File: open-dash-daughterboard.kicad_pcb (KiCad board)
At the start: 2 copper layers, 165.5 x 107.3 mm, 161 parts, among them J4 Conn_02x06_Odd_Even, P1 CONN_01X04, P2 CONN_01X02, P4 CONN_01X04, Q1 Q_NPN_BEC, Q2 Q_NJFET_DGS, Q3 Q_NJFET_DGS, Q4 Q_NPN_BCE, Q5 Q_PNP_BCE, U1 LM2576-ADJ, U10 Power-Monitor-INA219, U11 TDA7297, U12 Si4740, U13 A2235-H, U14 molex-2x4-5.7mm, U15 radio-housing-mounts, U16 molex-2x4-5.7mm, U17 USB_IC-CP2104, U18 74LVC1G17SE-7, U19 OPA1662, U2 LM2576-ADJ, U3 LM2576-ADJ, U4 LM2576-ADJ, U5 REG-3.3v, U6 ESP-WROOM-32, U7 molex-2x4-5.7mm, U8 MCP2551-I_SN, U9 SI7020-A20

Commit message: update
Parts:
- moved U14 5.23 mm to (141.9, 121.5)
- moved R5 1.00 mm to (107.9, 53.0)
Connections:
- U11 pad 14: /FL_AUDIO_OUT- -> /FR_AUDIO_OUT-
- U14 pad 2: /FL_AUDIO_OUT+ -> /FR_AUDIO_OUT+
- U14 pad 3: /FR_AUDIO_OUT+ -> /FL_AUDIO_OUT+
- U14 pad 5: /FL_AUDIO_OUT- -> /FR_AUDIO_OUT-
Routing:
- net /5V: track 54.0 -> 221.7 mm
- net /SOFT_POWER: track 14.4 -> 181.8 mm, vias 0 -> 5
- net /3v3: track 146.9 -> 310.0 mm, vias 0 -> 7
- net /SDA: track 16.9 -> 159.1 mm, vias 2 -> 14
- net /SCL: track 10.7 -> 127.6 mm, vias 0 -> 8
- net /PROG: track 6.29 -> 99.8 mm, vias 0 -> 3
- net /EN_AUDIO: track 0.00 -> 79.9 mm, vias 0 -> 2
- net /FACTORY: track 4.10 -> 63.1 mm, vias 0 -> 2
- net /AUDIO_POWER: track 52.4 -> 109.0 mm, vias 0 -> 1
- net /EN_MAIN: track 13.1 -> 68.2 mm, vias 0 -> 2
- net /CAN_RX: track 0.00 -> 52.5 mm, vias 0 -> 2
- net /FM Radio/am_passive_ant_en: track 4.00 -> 49.4 mm, vias 0 -> 2
- net /RXD: track 0.00 -> 43.9 mm, vias 0 -> 2
- net /STBY_AUDIO: track 0.00 -> 43.1 mm, vias 0 -> 2
- net /BATTERY: track 151.6 -> 193.9 mm, vias 0 -> 2
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
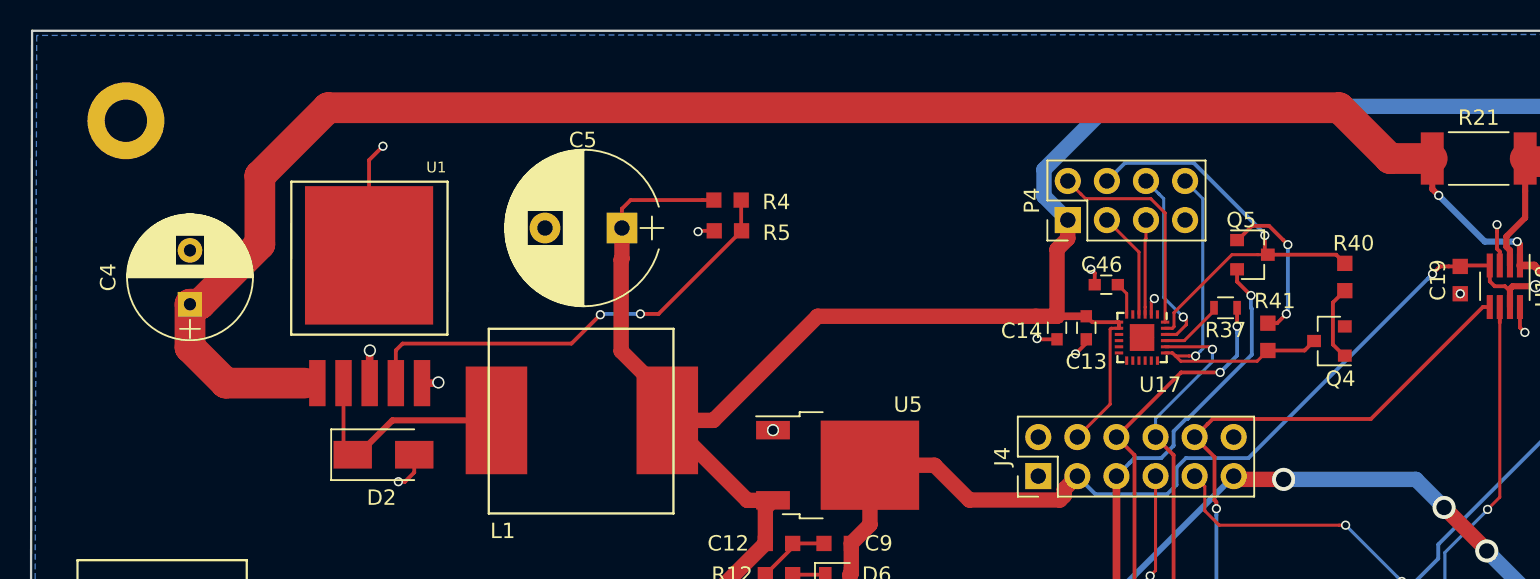
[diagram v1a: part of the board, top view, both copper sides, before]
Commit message: rearranged traces
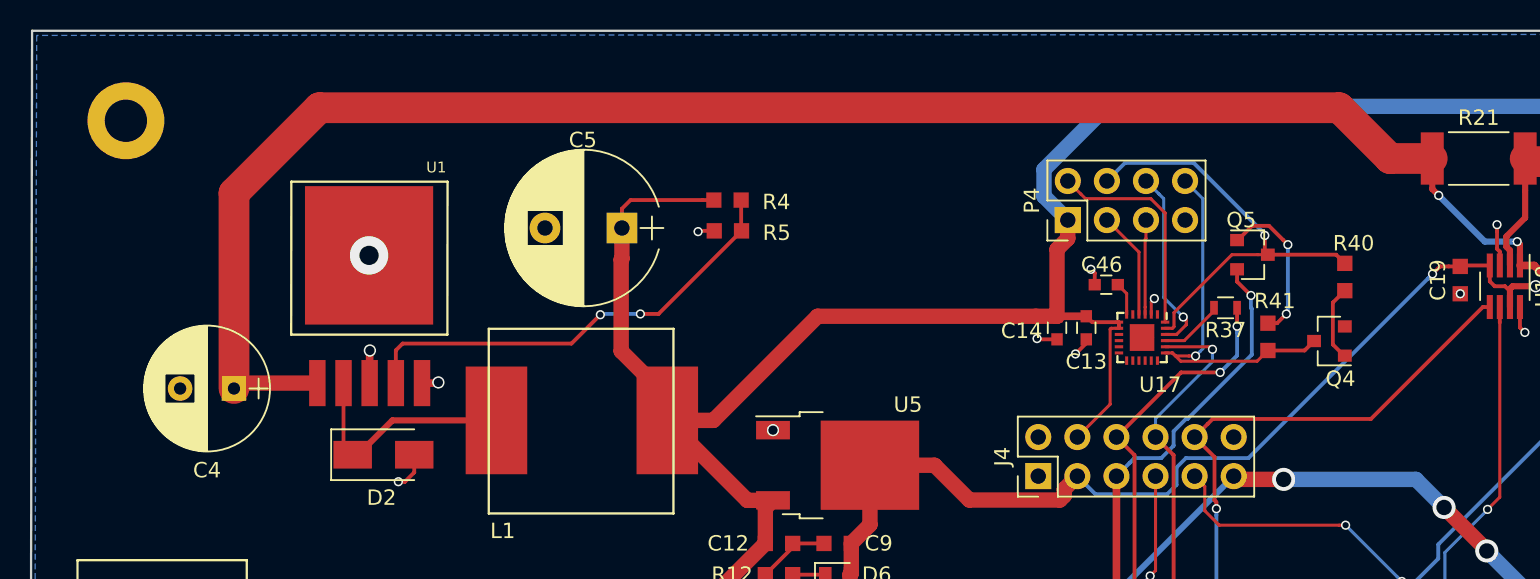
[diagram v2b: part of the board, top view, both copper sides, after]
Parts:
- moved C4 6.18 mm to (75.8, 63.2), turned to 180 degrees
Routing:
- net AGND: track 155.5 -> 148.0 mm
- net /BATTERY: track 193.9 -> 192.5 mm

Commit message: update
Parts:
- moved R13 2.42 mm to (151.0, 94.9), turned to 0 degrees
- moved L5 1.33 mm to (213.9, 123.9)
- moved R14 1.21 mm to (151.0, 92.4), turned to 0 degrees
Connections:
- AMF_Antenna1 pad 2: GNDA -> AGND
- C22 pad 1: /AUDIO_POWER -> AGND
- C22 pad 2: AGND -> /AUDIO_POWER
- GPS_ANT1 pad 2: GNDA -> AGND
- U14 pad 5: /FR_AUDIO_OUT- -> /FL_AUDIO_OUT-
- U14 pad 8: /FL_AUDIO_OUT- -> /FR_AUDIO_OUT-
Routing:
- net /3v3: track 310.0 -> 400.2 mm, vias 7 -> 11
- net /EN_DISPLAY: track 13.2 -> 62.5 mm, vias 2 -> 6
- net /CAN_TX: track 0.00 -> 49.2 mm, vias 0 -> 4
- net /EN_ESP: track 16.5 -> 57.6 mm, vias 2 -> 6
- net /BATTERY: track 192.5 -> 233.5 mm
- net /FR_AUDIO_OUT-: track 0.00 -> 39.8 mm
- net /FL_AUDIO_OUT+: track 0.46 -> 38.2 mm
- net /FR_AUDIO_OUT+: track 0.00 -> 31.8 mm
- net /FL_AUDIO_OUT-: track 0.00 -> 31.5 mm
- net /SDA: track 159.1 -> 129.8 mm, vias 14 -> 9
- net /STBY_AUDIO: track 43.1 -> 60.3 mm, vias 2 -> 8
- net /EN_AUDIO: track 79.9 -> 89.6 mm
- net /CAN_RX: track 52.5 -> 61.8 mm, vias 2 -> 6
- net Net-(D2-Pad1): track 15.2 -> 21.0 mm
- net /V_MAIN: track 36.3 -> 31.0 mm
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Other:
- board text added: "3v3"
- board text added: "5V"
- board text added: "BATT"
- board text added: "CAM +"
- board text added: "CAM --"
- board text added: "CAM_S"
- board text added: "CAN +"
- board text added: "CAN -"
- board text added: "DCD"
- board text added: "DSR"
- board text added: "DTR"
- board text added: "D_N"
- board text added: "D_P"
- board text added: "FACT"
- board text added: "FL OUT +"
- board text added: "FL OUT -"
- board text added: "FR OUT +"
- board text added: "FR OUT -"
- board text added: "GND"
- board text added: "IN2"
- board text added: "L MAIN"
- board text added: "NC"
- board text added: "OUT2+"
- board text added: "OUT2-"
- board text added: "PROG"
- board text added: "R MAIN"
- board text added: "RTS"
- board text added: "RXD"
- board text added: "SCL"
- board text added: "SDA"
- board text added: "SOFT P"
- board text added: "SOFT_P"
- board text added: "TXD"
- board text added: "VCC"

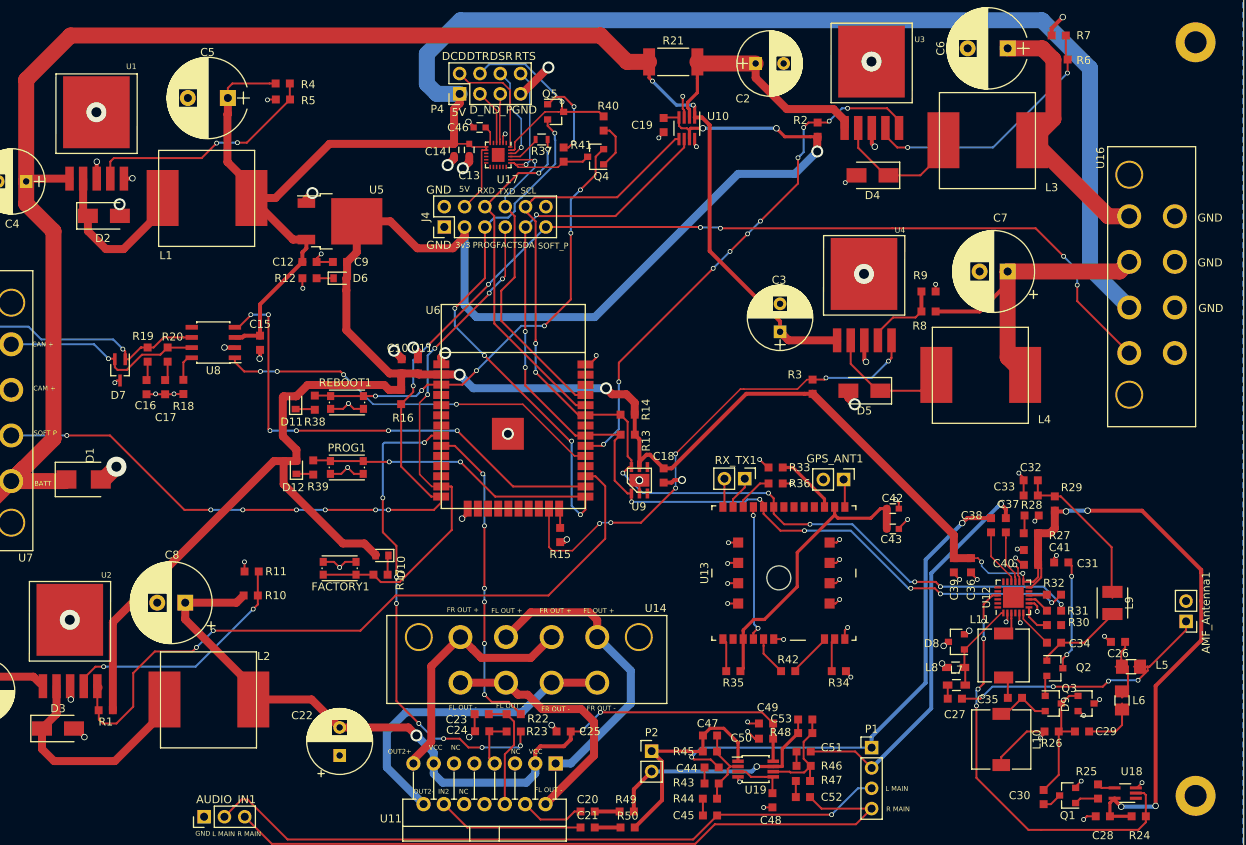
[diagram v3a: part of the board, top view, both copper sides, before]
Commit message: final update silk screen
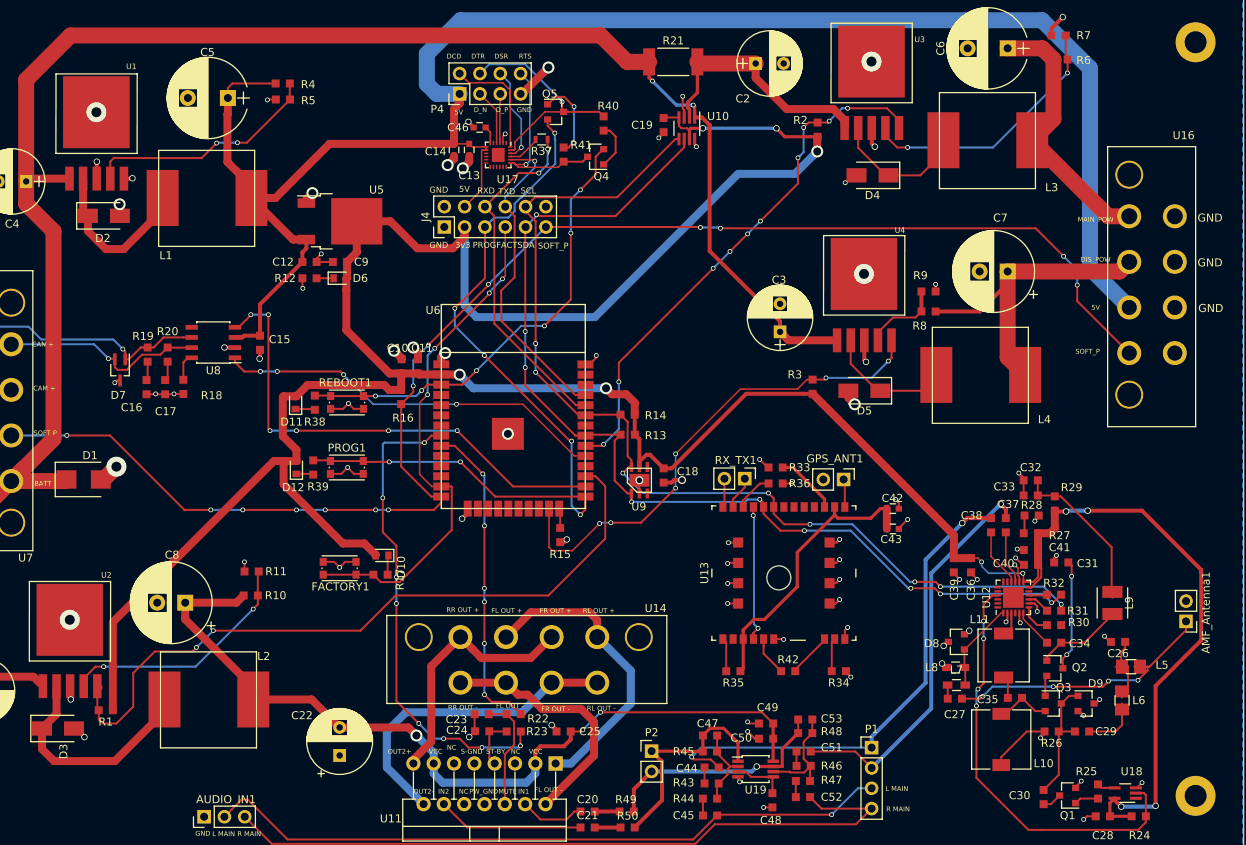
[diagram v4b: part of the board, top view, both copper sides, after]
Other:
- board text added: "DIS_POW"
- board text added: "IN1"
- board text added: "MAIN_POW"
- board text added: "MUTE"
- board text added: "PW_GND"
- board text added: "RL OUT +"
- board text added: "RL OUT -"
- board text added: "RR OUT +"
- board text added: "RR OUT -"
- board text added: "S-GND"
- board text added: "ST-BY"
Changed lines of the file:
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@@
   (general
     (thickness 1.6)
-    (drawings 56)
+    (drawings 65)
     (tracks 1520)
     (zones 0)
@@
     (tags "resistor handsolder")
     (attr smd)
-    (fp_text reference R48 (at 3.1 0.1 180) (layer F.SilkS)
+    (fp_text reference R48 (at -3.3 0.2 180) (layer F.SilkS)
       (effects (font (size 1 1) (thickness 0.15)))
     )
@@
     (tags "Diode SMB (DO-214AA)")
     (attr smd)
-    (fp_text reference D1 (at 0.8 -3 -90) (layer F.SilkS)
+    (fp_text reference D1 (at 0.8 -3 180) (layer F.SilkS)
       (effects (font (size 1 1) (thickness 0.15)))
     )
@@
     (tags "capacitor handsolder")
     (attr smd)
-    (fp_text reference C15 (at -2.33 0) (layer F.SilkS)
+    (fp_text reference C15 (at -0.41 -2.45) (layer F.SilkS)
       (effects (font (size 1 1) (thickness 0.15)))
     )
@@
     (tags "capacitor handsolder")
     (attr smd)
-    (fp_text reference C16 (at 2.29 0.13) (layer F.SilkS)
+    (fp_text reference C16 (at 2.54 1.86) (layer F.SilkS)
       (effects (font (size 1 1) (thickness 0.15)))
     )
@@
     (tags "capacitor handsolder")
     (attr smd)
-    (fp_text reference C17 (at 3.78 -0.07) (layer F.SilkS)
+    (fp_text reference C17 (at 3.04 -0.07) (layer F.SilkS)
       (effects (font (size 1 1) (thickness 0.15)))
     )
@@
     (tags "capacitor handsolder")
     (attr smd)
-    (fp_text reference C18 (at -2.4 0) (layer F.SilkS)
+    (fp_text reference C18 (at -0.5 -3) (layer F.SilkS)
       (effects (font (size 1 1) (thickness 0.15)))
     )
@@
     (tags "resistor handsolder")
     (attr smd)
-    (fp_text reference R13 (at 2.2875 0.762 90) (layer F.SilkS)
+    (fp_text reference R13 (at 3.4875 0.1 180) (layer F.SilkS)
       (effects (font (size 1 1) (thickness 0.15)))
     )
@@
     (tags "resistor handsolder")
     (attr smd)
-    (fp_text reference R14 (at 2.2875 -0.635 90) (layer F.SilkS)
+    (fp_text reference R14 (at 3.5 0.1 180) (layer F.SilkS)
       (effects (font (size 1 1) (thickness 0.15)))
     )
@@
     (tags "resistor handsolder")
     (attr smd)
-    (fp_text reference R18 (at 2.41 -0.01) (layer F.SilkS)
+    (fp_text reference R18 (at 1.07 -3.53) (layer F.SilkS)
       (effects (font (size 1 1) (thickness 0.15)))
     )
@@
     (tags "resistor handsolder")
     (attr smd)
-    (fp_text reference R20 (at -2.22 -0.6) (layer F.SilkS)
+    (fp_text reference R20 (at -2.8875 0) (layer F.SilkS)
       (effects (font (size 1 1) (thickness 0.15)))
     )
@@
     (tags "Diode SMA (DO-214AC)")
     (attr smd)
-    (fp_text reference D3 (at 0 -2.5) (layer F.SilkS)
+    (fp_text reference D3 (at 0.704 2.871 90) (layer F.SilkS)
       (effects (font (size 1 1) (thickness 0.15)))
     )
@@
   (module open-automation:molex-2x4-5.7mm (layer F.Cu)
     (at 215 72.9 90)
-    (fp_text reference U16 (at 12.6 -4.9 90) (layer F.SilkS)
+    (fp_text reference U16 (at 15.4 5.5 180) (layer F.SilkS)
       (effects (font (size 1 1) (thickness 0.15)))
     )
@@
     (tags "Choke SMD")
     (attr smd)
-    (fp_text reference L10 (at 0 -4.45 270) (layer F.SilkS)
+    (fp_text reference L10 (at 3 -5.3) (layer F.SilkS)
       (effects (font (size 1 1) (thickness 0.15)))
     )
@@
     (tags SOT-23)
     (attr smd)
-    (fp_text reference Q2 (at 3.6 -0.1) (layer F.SilkS)
+    (fp_text reference Q2 (at 3.1 -0.1) (layer F.SilkS)
       (effects (font (size 1 1) (thickness 0.15)))
     )
@@
     (tags SOT-23)
     (attr smd)
-    (fp_text reference Q3 (at 2 -1.9) (layer F.SilkS)
+    (fp_text reference Q3 (at 1.3 -2) (layer F.SilkS)
       (effects (font (size 1 1) (thickness 0.15)))
     )
@@
     (tags SOT-23)
     (attr smd)
-    (fp_text reference D9 (at -2.6 0.1 -270) (layer F.SilkS)
+    (fp_text reference D9 (at 1.2 -2.5 -180) (layer F.SilkS)
       (effects (font (size 1 1) (thickness 0.15)))
     )
@@
     (tags "capacitor handsolder")
     (attr smd)
-    (fp_text reference C53 (at -3 -0.1) (layer F.SilkS)
+    (fp_text reference C53 (at 3.3 -0.1) (layer F.SilkS)
       (effects (font (size 1 1) (thickness 0.15)))
     )
@@
     (pad M thru_hole circle (at 10.5 -1.3) (size 3.5 3.5) (drill 3) (layers *.Cu *.Mask))
   )
+  (gr_text MAIN_POW (at 209.5 68) (layer F.SilkS)
+    (effects (font (size 0.6 0.6) (thickness 0.15)))
+  )
+  (gr_text DIS_POW (at 209.5 73) (layer F.SilkS)
+    (effects (font (size 0.6 0.6) (thickness 0.15)))
+  )
+  (gr_text 5V (at 209.5 79) (layer F.SilkS)
+    (effects (font (size 0.6 0.6) (thickness 0.15)))
+  )
+  (gr_text SOFT_P (at 208.5 84.5) (layer F.SilkS)
+    (effects (font (size 0.6 0.6) (thickness 0.15)))
+  )
+  (gr_text S-GND (at 131.5 134.5) (layer F.SilkS)
+    (effects (font (size 0.6 0.6) (thickness 0.15)))
+  )
+  (gr_text ST-BY (at 134.5 134.5) (layer F.SilkS)
+    (effects (font (size 0.6 0.6) (thickness 0.15)))
+  )
+  (gr_text IN1 (at 138 139.5) (layer F.SilkS)
+    (effects (font (size 0.6 0.6) (thickness 0.15)))
+  )
+  (gr_text MUTE (at 136 139.5) (layer F.SilkS)
+    (effects (font (size 0.6 0.6) (thickness 0.15)))
+  )
+  (gr_text PW_GND (at 133 139.5) (layer F.SilkS)
+    (effects (font (size 0.6 0.6) (thickness 0.15)))
+  )
   (gr_text OUT2+ (at 122.5 134.5) (layer F.SilkS)
     (effects (font (size 0.6 0.6) (thickness 0.15)))
@@
     (effects (font (size 0.6 0.6) (thickness 0.15)))
   )
-  (gr_text VCC (at 127 134) (layer F.SilkS)
+  (gr_text VCC (at 127 134.5) (layer F.SilkS)
     (effects (font (size 0.6 0.6) (thickness 0.15)))
   )
-  (gr_text NC (at 129.5 134) (layer F.SilkS)
+  (gr_text NC (at 129 134) (layer F.SilkS)
     (effects (font (size 0.6 0.6) (thickness 0.15)))
   )
@@
     (effects (font (size 0.6 0.6) (thickness 0.15)))
   )
-  (gr_text "FL OUT -" (at 130.4 129) (layer F.SilkS)
+  (gr_text "RR OUT -" (at 130.4 129) (layer F.SilkS)
     (effects (font (size 0.6 0.6) (thickness 0.15)))
   )
@@
     (effects (font (size 0.6 0.6) (thickness 0.15)))
   )
-  (gr_text "FR OUT -" (at 147.7 129.1) (layer F.SilkS)
+  (gr_text "RL OUT -" (at 147.7 129.1) (layer F.SilkS)
     (effects (font (size 0.6 0.6) (thickness 0.15)))
   )
-  (gr_text "FL OUT +" (at 147.4 116.9) (layer F.SilkS)
+  (gr_text "RL OUT +" (at 147.4 116.9) (layer F.SilkS)
     (effects (font (size 0.6 0.6) (thickness 0.15)))
   )
@@
     (effects (font (size 0.6 0.6) (thickness 0.15)))
   )
-  (gr_text "FR OUT +" (at 130.4 116.8) (layer F.SilkS)
+  (gr_text "RR OUT +" (at 130.4 116.8) (layer F.SilkS)
     (effects (font (size 0.6 0.6) (thickness 0.15)))
   )
@@
   )
   (gr_text GND (at 127.4 71.2) (layer F.SilkS)
-    (effects (font (size 1 1) (thickness 0.25)))
+    (effects (font (size 0.75 0.75) (thickness 0.1875)))
   )
   (gr_text GND (at 127.4 64.3) (layer F.SilkS)
-    (effects (font (size 1 1) (thickness 0.25)))
+    (effects (font (size 0.75 0.75) (thickness 0.1875)))
   )
   (gr_text GND (at 64.1 100.8) (layer F.SilkS)
@@
   )
   (gr_text GND (at 138.1 54.3) (layer F.SilkS)
-    (effects (font (size 1 1) (thickness 0.25)))
+    (effects (font (size 0.6 0.6) (thickness 0.15)))
   )
   (gr_text D_P (at 135.3 54.3) (layer F.SilkS)
-    (effects (font (size 1 1) (thickness 0.25)))
+    (effects (font (size 0.6 0.6) (thickness 0.15)))
   )
   (gr_text D_N (at 132.6 54.3) (layer F.SilkS)
-    (effects (font (size 1 1) (thickness 0.25)))
+    (effects (font (size 0.6 0.6) (thickness 0.15)))
   )
   (gr_text 5V (at 129.9 54.6) (layer F.SilkS)
-    (effects (font (size 1 1) (thickness 0.25)))
+    (effects (font (size 0.6 0.6) (thickness 0.15)))
   )
   (gr_text DSR (at 135.2 47.6) (layer F.SilkS)
-    (effects (font (size 1 1) (thickness 0.25)))
+    (effects (font (size 0.6 0.6) (thickness 0.15)))
   )
   (gr_text DTR (at 132.3 47.6) (layer F.SilkS)
-    (effects (font (size 1 1) (thickness 0.25)))
+    (effects (font (size 0.6 0.6) (thickness 0.15)))
   )
   (gr_text DCD (at 129.3 47.6) (layer F.SilkS)
-    (effects (font (size 1 1) (thickness 0.25)))
+    (effects (font (size 0.6 0.6) (thickness 0.15)))
   )
   (gr_text "RTS\n" (at 138.2 47.6) (layer F.SilkS)
-    (effects (font (size 1 1) (thickness 0.25)))
+    (effects (font (size 0.6 0.6) (thickness 0.15)))
   )
   (gr_line (start 62.7 40) (end 62.5 147.3) (layer Edge.Cuts) (width 0.15))

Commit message: finalizing board
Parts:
- moved C25 22.1 mm to (120.9, 132.6), turned to 270 degrees
- moved C23 0.90 mm to (132.6, 130.7)
- moved R22 0.90 mm to (136.6, 130.7)
- moved R23 0.90 mm to (136.6, 132.9)
- moved C24 0.90 mm to (132.7, 132.9)
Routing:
- net AGND: track 147.5 -> 152.7 mm, vias 88 -> 87
- net /AUDIO_POWER: track 105.0 -> 108.9 mm, vias 3 -> 2
- net Net-(C26-Pad1): track 11.6 -> 10.1 mm
- net Net-(C23-Pad1): track 14.3 -> 13.4 mm
- net /STBY_AUDIO: track 60.3 -> 59.5 mm
- net /MUTE_AUDIO: track 39.9 -> 40.7 mm
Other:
- board text added: "BATTERY"
- board text added: "CAM-"
- board text added: "CAMERA+"
- board text added: "CAN+"
- board text added: "CAN-"
- board text added: "DISPLAY+"
- board text added: "FL+"
- board text added: "FL-"
- board text added: "FR+"
- board text added: "FR-"
- board text added: "L"
- board text added: "L_FM"
- board text added: "L_MAIN"
- board text added: "MAIN+"
- board text added: "OUT1+"
- board text added: "OUT1-"
- board text added: "PWR"
- board text added: "R"
- board text added: "RL+"
- board text added: "RL-"
- board text added: "RR+"
- board text added: "RR-"
- board text added: "R_FM"
- board text added: "R_MAIN"
- board text added: "SOFT_PWR"
- board text added: "STBY"
- board text removed: "BATT"
- board text removed: "CAM +"
- board text removed: "CAM --"
- board text removed: "CAN +"
- board text removed: "CAN -"
- board text removed: "DIS_POW"
- board text removed: "FL OUT +"
- board text removed: "FL OUT -"
- board text removed: "FR OUT +"
- board text removed: "FR OUT -"
- board text removed: "L MAIN"
- board text removed: "MAIN_POW"
- board text removed: "NC"
- board text removed: "PW_GND"
- board text removed: "R MAIN"
- board text removed: "RL OUT +"
- board text removed: "RL OUT -"
- board text removed: "RR OUT +"
- board text removed: "RR OUT -"
- board text removed: "S-GND"
- board text removed: "SOFT P"
- board text removed: "SOFT_P"
- board text removed: "ST-BY"
- board text removed: "VCC"
